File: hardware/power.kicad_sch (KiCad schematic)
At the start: 21 parts

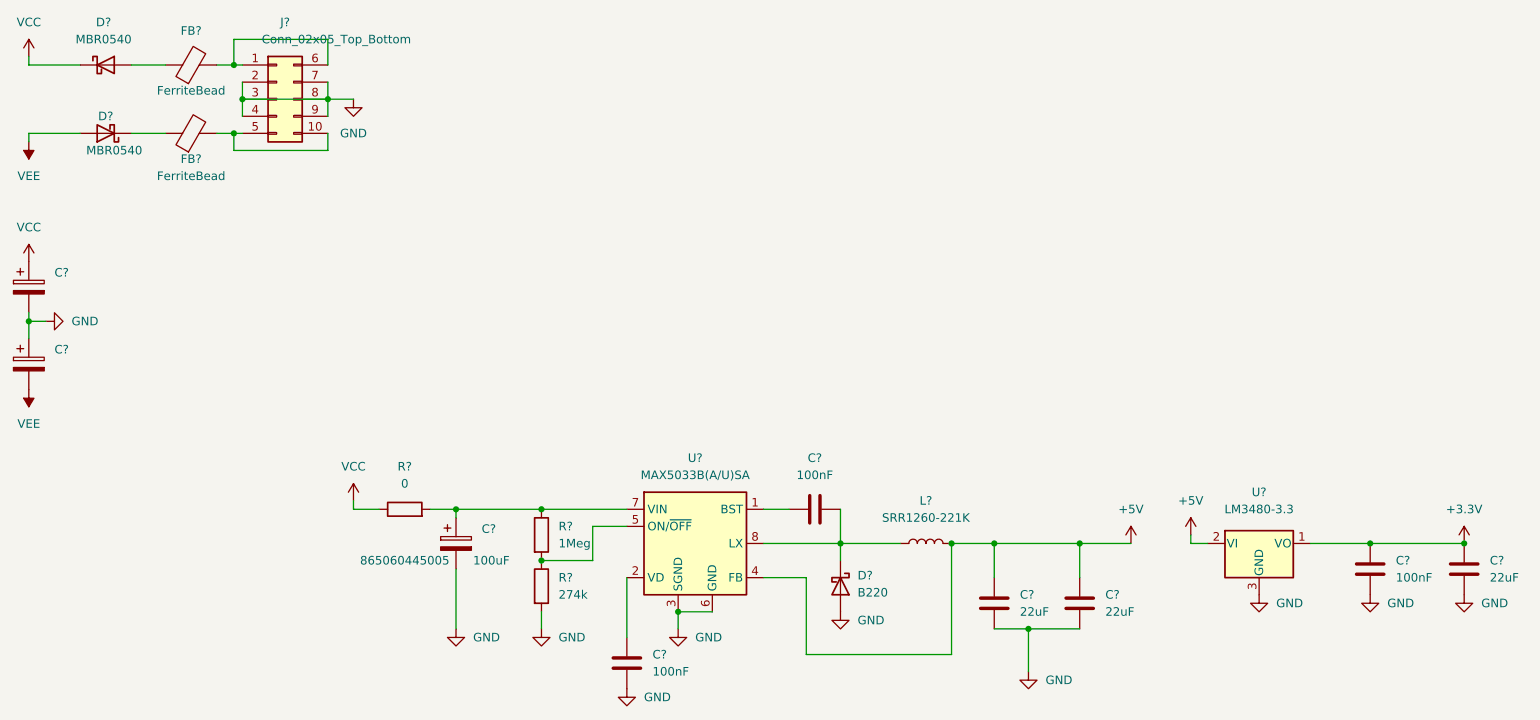
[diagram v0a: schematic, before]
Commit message: MAX5715BAUD lib added
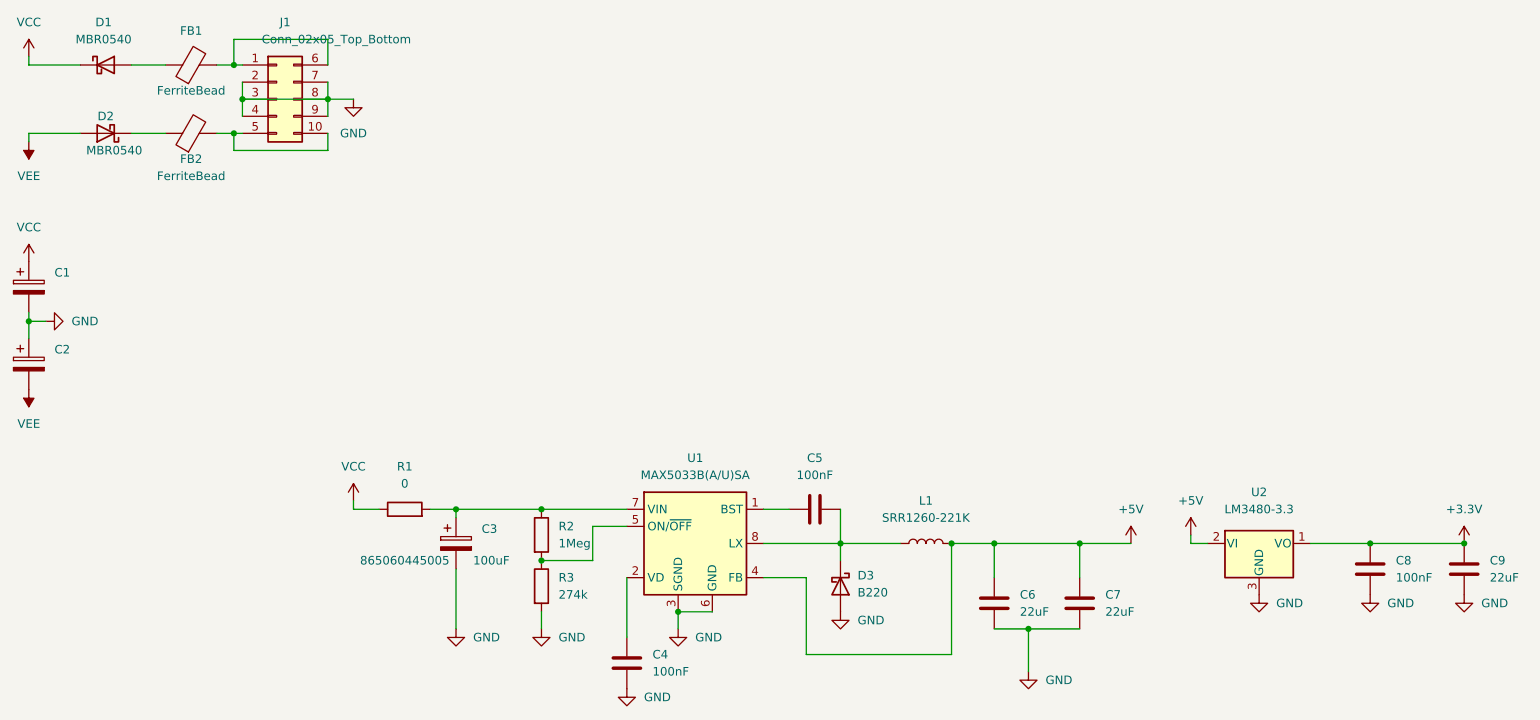
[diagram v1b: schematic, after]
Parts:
- gave numbers to parts that had none: 21
